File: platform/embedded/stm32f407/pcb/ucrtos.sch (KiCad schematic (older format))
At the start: 1 part

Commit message: stm32f4: pcb: migrate kicad project
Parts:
- J?: symbol nes_gamepad_02x03 -> ucrtos-rescue:nes_gamepad_02x03
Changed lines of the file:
@@
-EESchema Schematic File Version 2
-LIBS:power
-LIBS:device
-LIBS:switches
-LIBS:relays
-LIBS:motors
-LIBS:transistors
-LIBS:conn
-LIBS:linear
-LIBS:regul
-LIBS:74xx
-LIBS:cmos4000
-LIBS:adc-dac
-LIBS:memory
-LIBS:xilinx
-LIBS:microcontrollers
-LIBS:dsp
-LIBS:microchip
-LIBS:analog_switches
-LIBS:motorola
-LIBS:texas
-LIBS:intel
-LIBS:audio
-LIBS:interface
-LIBS:digital-audio
-LIBS:philips
-LIBS:display
-LIBS:cypress
-LIBS:siliconi
-LIBS:opto
-LIBS:atmel
-LIBS:contrib
-LIBS:valves
-EELAYER 25 0
+EESchema Schematic File Version 4
+LIBS:ucrtos-cache
+EELAYER 26 0
 EELAYER END
 $Descr A4 11693 8268
@@
 $EndDescr
 $Comp
-L nes_gamepad_02x03 J?
+L ucrtos-rescue:nes_gamepad_02x03 J?
 U 1 1 5A4D2E55
 P 1400 1250
@@
 $EndComp
 $Comp
-L GND #PWR?
+L power:GND #PWR?
 U 1 1 5A4D2EC1
 P 1100 1650
@@
 	1100 1350 1100 1650
 $Comp
-L VCC #PWR?
+L power:VCC #PWR?
 U 1 1 5A4D2EAB
 P 1100 1050

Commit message: assign footprints / generate netlist
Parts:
- added J2: STM32F4_Discovery_Header, w_conn_misc:stm32f4_discovery_header, symbol w_connectors:STM32F4_Discovery_Header
- J1: renamed from J?; footprint (none) -> Connector_IDC:IDC-Header_2x03_P2.54mm_Vertical
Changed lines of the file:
@@
 $EndDescr
 $Comp
-L ucrtos-rescue:nes_gamepad_02x03 J?
+L ucrtos-rescue:nes_gamepad_02x03 J1
 U 1 1 5A4D2E55
 P 1400 1250
-F 0 "J?" H 1450 1450 50  0000 C CNN
+F 0 "J1" H 1450 1450 50  0000 C CNN
 F 1 "nes_gamepad_02x03" H 1450 1050 50  0000 C CNN
-F 2 "" H 1400 1250 50  0001 C CNN
+F 2 "Connector_IDC:IDC-Header_2x03_P2.54mm_Vertical" H 1400 1250 50  0001 C CNN
 F 3 "" H 1400 1250 50  0001 C CNN
 	1    1400 1250
@@
 $EndComp
 $Comp
-L power:GND #PWR?
+L power:GND #PWR0101
 U 1 1 5A4D2EC1
 P 1100 1650
-F 0 "#PWR?" H 1100 1400 50  0001 C CNN
+F 0 "#PWR0101" H 1100 1400 50  0001 C CNN
 F 1 "GND" H 1100 1500 50  0000 C CNN
 F 2 "" H 1100 1650 50  0001 C CNN
@@
 	1100 1350 1100 1650
 $Comp
-L power:VCC #PWR?
+L power:VCC #PWR0102
 U 1 1 5A4D2EAB
 P 1100 1050
-F 0 "#PWR?" H 1100 900 50  0001 C CNN
+F 0 "#PWR0102" H 1100 900 50  0001 C CNN
 F 1 "VCC" H 1100 1200 50  0000 C CNN
 F 2 "" H 1100 1050 50  0001 C CNN
@@
 	1    0    0    -1
 $EndComp
+$Comp
+L w_connectors:STM32F4_Discovery_Header J2
+U 1 1 5C40F60D
+P 4350 2600
+F 0 "J2" H 4350 4193 60  0000 C CNN
+F 1 "STM32F4_Discovery_Header" H 4350 4087 60  0000 C CNN
+F 2 "w_conn_misc:stm32f4_discovery_header" H 4350 3981 60  0000 C CNN
+F 3 "" H 4350 2950 60  0000 C CNN
+	1    4350 2600
+	1    0    0    -1
+$EndComp

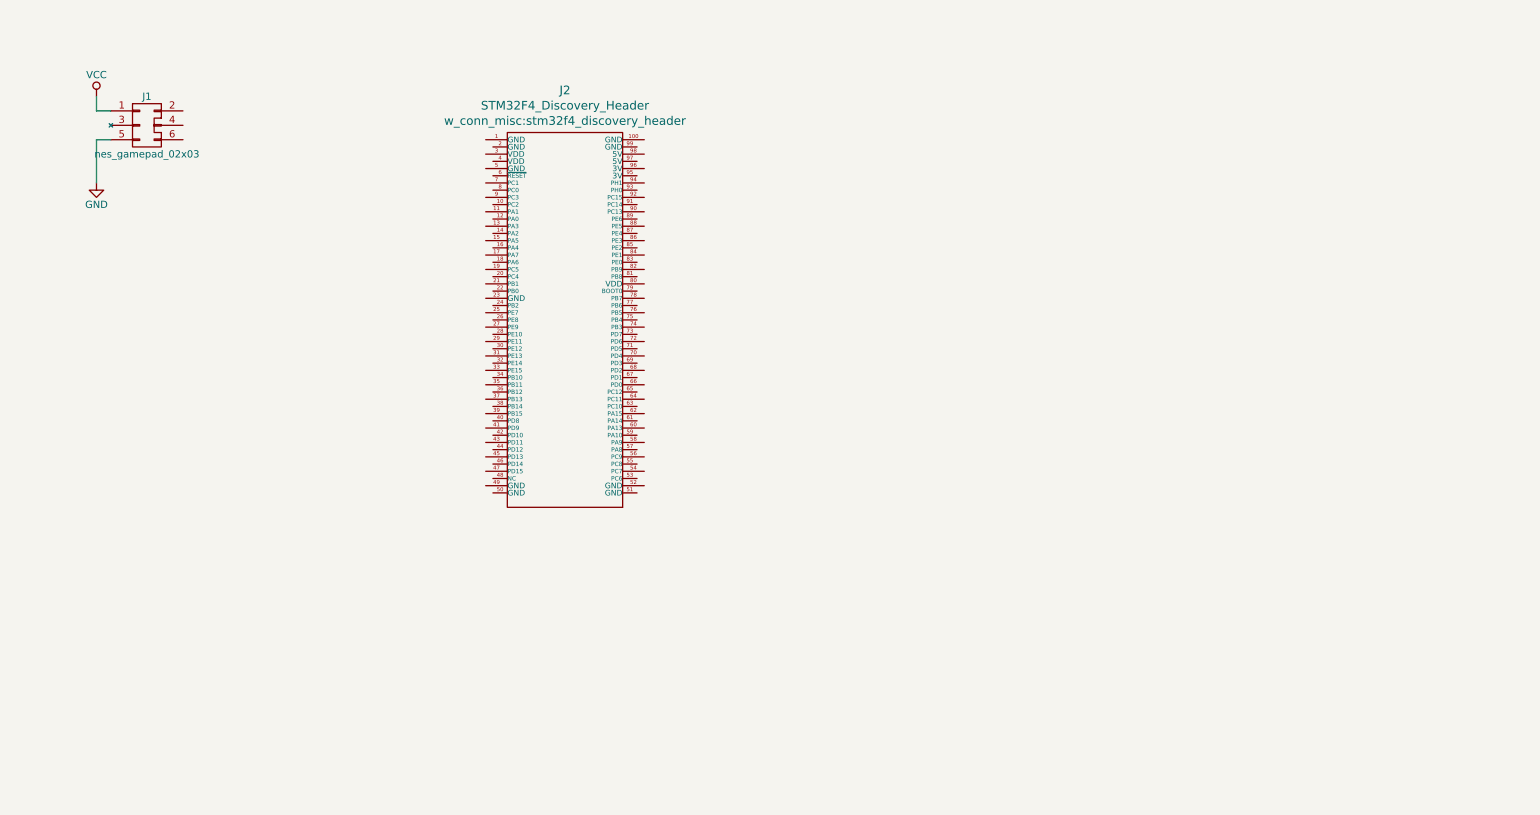
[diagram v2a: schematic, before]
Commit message: platform stm32f4: pcb: add HY32D symbol + wire SD card connector
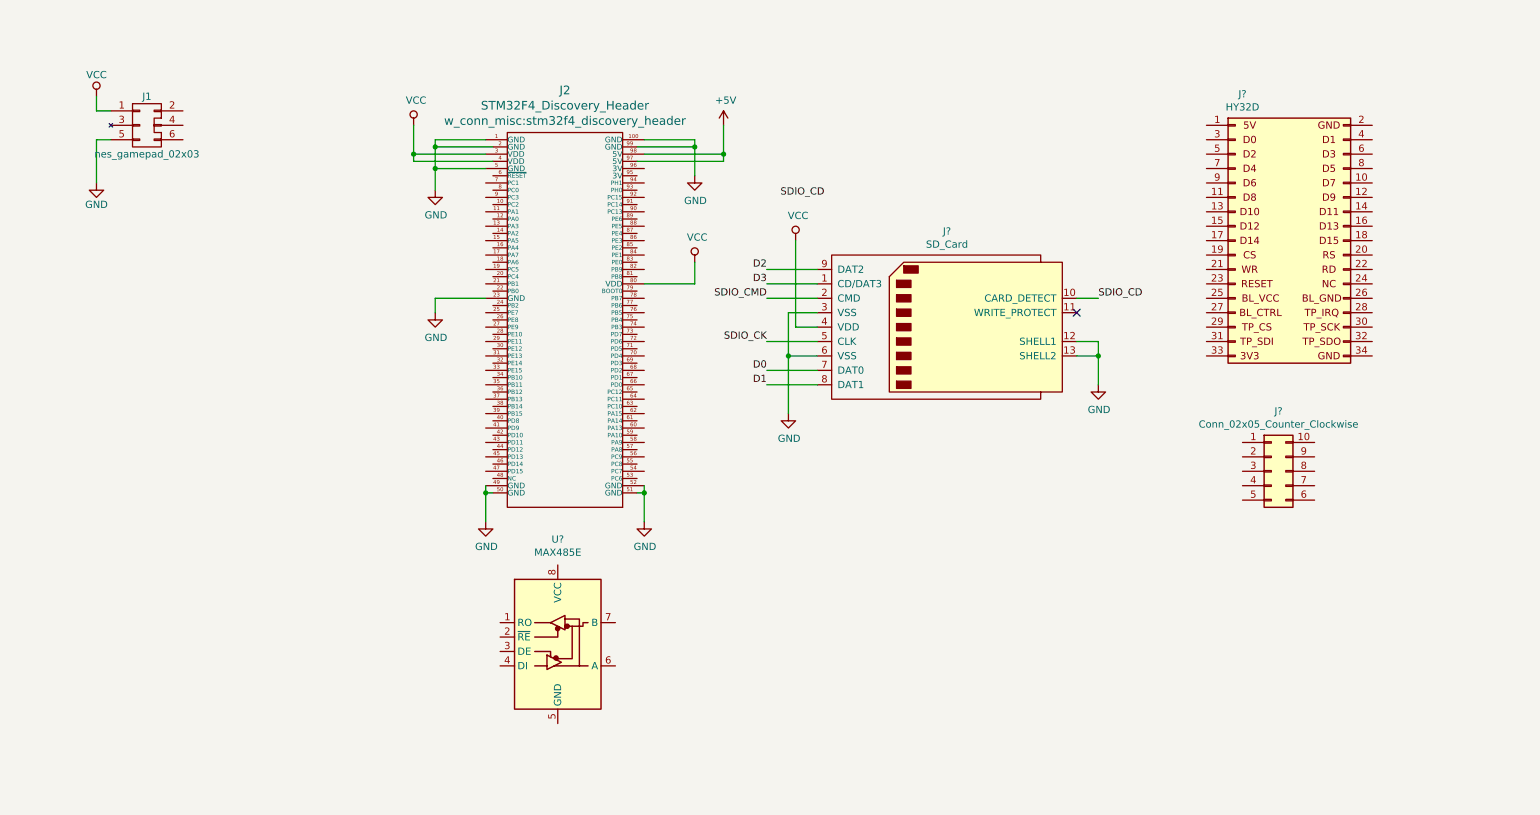
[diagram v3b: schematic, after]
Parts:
- added J?: Conn_02x05_Counter_Clockwise, symbol Connector_Generic:Conn_02x05_Counter_Clockwise
- added J?: HY32D, symbol hy32d:HY32D
- added J?: SD_Card, symbol Connector:SD_Card
- added U?: MAX485E, symbol Interface_UART:MAX485E
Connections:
- net GND: now also J2.1 (GND), J2.100 (GND), J2.2 (GND), J2.23 (GND), J2.49 (GND), J2.5 (GND), J2.50 (GND), J2.51 (GND), J2.52 (GND), J2.99 (GND), J?.12 (SHELL1), J?.13 (SHELL2), J?.3 (VSS), J?.6 (VSS)
- net VCC: now also J2.3 (VDD), J2.4 (VDD), J2.80 (VDD), J?.4 (VDD)
- net +5V: now reaches J2.97 (5V)
- net +5V: now also J2.98 (5V)
- new net D0: J?.7 (DAT0)
- new net D1: J?.8 (DAT1)
- new net D2: J?.9 (DAT2)
- new net D3: J?.1 (CD/DAT3)
- new net SDIO_CD: J?.10 (CARD_DETECT)
- new net SDIO_CK: J?.5 (CLK)
- new net SDIO_CMD: J?.2 (CMD)
- no-connect marks 0 -> 1

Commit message: platform stm32f4: pcb: add FTDI symbol + wire FTDI + LCD
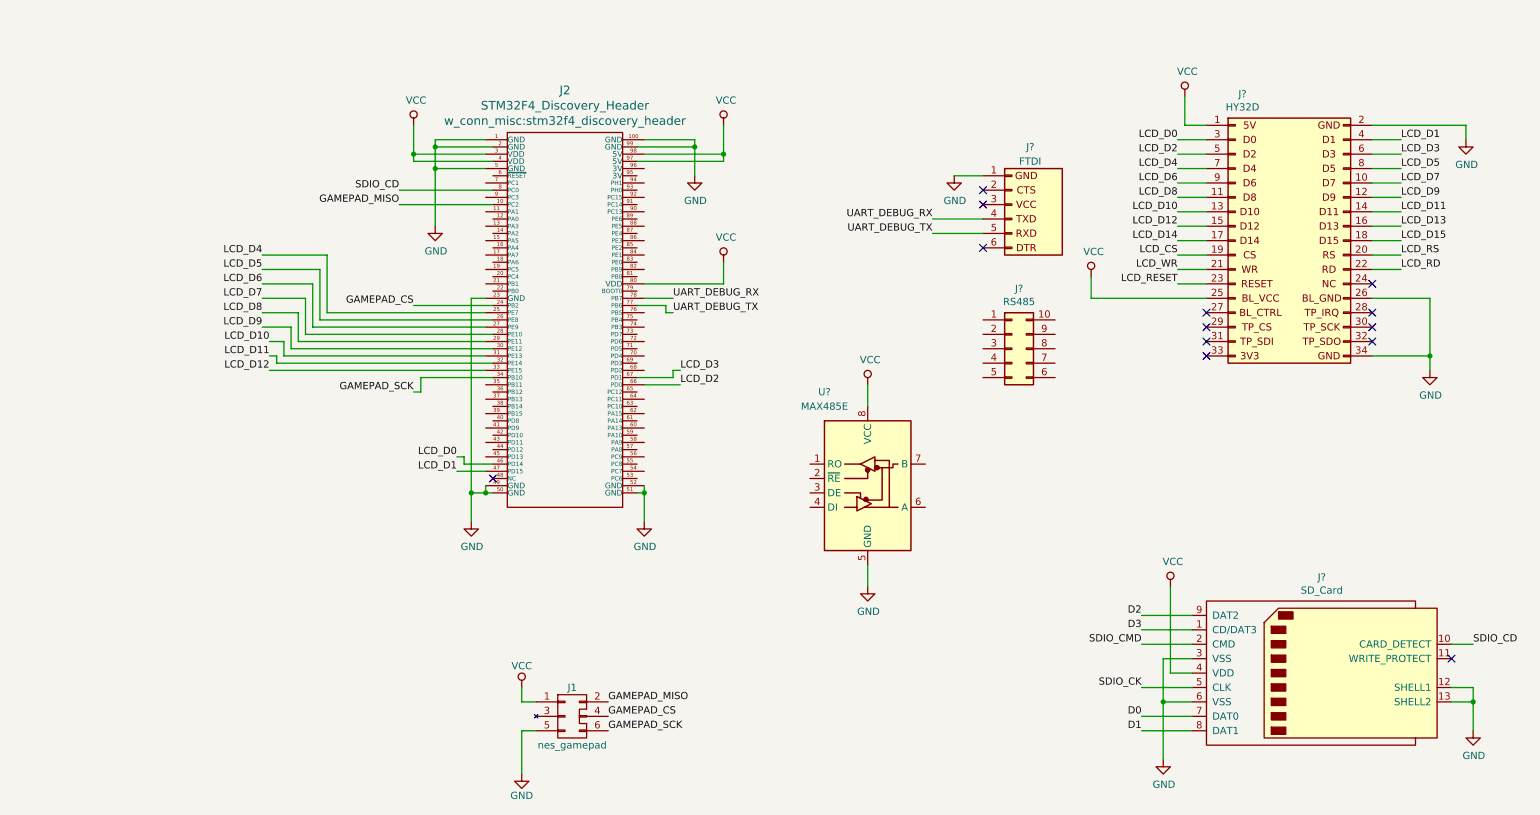
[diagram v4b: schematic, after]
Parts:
- added J?: FTDI, symbol ftdi:FTDI
- J1: value nes_gamepad_02x03 -> nes_gamepad
- J?: value Conn_02x05_Counter_Clockwise -> RS485
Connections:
- net +5V is gone; now on net VCC: J2.97 (5V), J2.98 (5V)
- net GND: now also J?.2 (D0), J?.26 (D15), J?.34 (GND), U?.5 (GND), J?.1 (Pin_1)
- net SDIO_CD: now also J2.8 (PC0)
- net VCC: now also J?.1 (5V), J?.25 (RS), U?.8 (VCC)
- net GAMEPAD_MISO: now reaches J1.2 (MISO)
- net GAMEPAD_MISO: now also J2.10 (PC2)
- net GAMEPAD_CS: now reaches J1.4 (LATCH)
- net GAMEPAD_CS: now also J2.24 (PB2)
- net GAMEPAD_SCK: now reaches J1.6 (SCK)
- net GAMEPAD_SCK: now also J2.34 (PB10)
- net LCD_D4: now reaches J2.25 (PE7)
- net LCD_D4: now also J?.7 (D10)
- net LCD_D5: now reaches J2.26 (PE8)
- net LCD_D5: now also J?.8 (D12)
- net LCD_D6: now reaches J2.27 (PE9)
- net LCD_D6: now also J?.9 (D14)
- net LCD_D7: now reaches J2.28 (PE10)
- net LCD_D7: now also J?.10 (CS)
- net LCD_D8: now reaches J2.29 (PE11)
- net LCD_D8: now also J?.11 (WR)
- net LCD_D9: now reaches J2.30 (PE12)
- net LCD_D9: now also J?.12 (RESET)
- net LCD_D10: now reaches J2.31 (PE13)
- net LCD_D10: now also J?.13 (BL_VDD)
- net LCD_D11: now reaches J2.32 (PE14)
- net LCD_D11: now also J?.14 (BL_CNT)
- net LCD_D12: now reaches J2.33 (PE15)
- net LCD_D12: now also J?.15 (TP_CS)
- net LCD_D0: now reaches J2.46 (PD14)
- net LCD_D0: now also J?.3 (D2)
- net LCD_D1: now reaches J2.47 (PD15)
- net LCD_D1: now also J?.4 (D4)
- net LCD_D2: now reaches J2.66 (PD0)
- net LCD_D2: now also J?.5 (D6)
- net LCD_D3: now reaches J2.67 (PD1)
- net LCD_D3: now also J?.6 (D8)
- net UART_DEBUG_TX: now reaches J2.77 (PB6)
- net UART_DEBUG_TX: now also J?.5 (Pin_5)
- net UART_DEBUG_RX: now reaches J2.78 (PB7)
- net UART_DEBUG_RX: now also J?.4 (Pin_4)
- net LCD_D13: now reaches J?.16 (TP_SI)
- net LCD_D14: now reaches J?.17 (3V3)
- net LCD_D15: now reaches J?.18 (GND)
- net LCD_CS: now reaches J?.19 (TP_SO)
- net LCD_RS: now reaches J?.20 (TP_SCK)
- net LCD_WR: now reaches J?.21 (TP_IRQ)
- net LCD_RD: now reaches J?.22 (BLGND)
- net LCD_RESET: now reaches J?.23 (NC)
- no-connect marks 1 -> 13
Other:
- moved on the sheet: J1, J?, U?
